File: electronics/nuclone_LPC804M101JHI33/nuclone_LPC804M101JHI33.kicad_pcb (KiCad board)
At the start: 2 copper layers, 50 x 50 mm, 42 parts, among them J1 JTAG_2X05, J2 TYPE-C-31-M-12, J3 nuclone_small_left, J4 nuclone_small_right, SW1 RESET, SW2 Bootloader, U1 MCP1702-MB, U2 TPESD0504C6

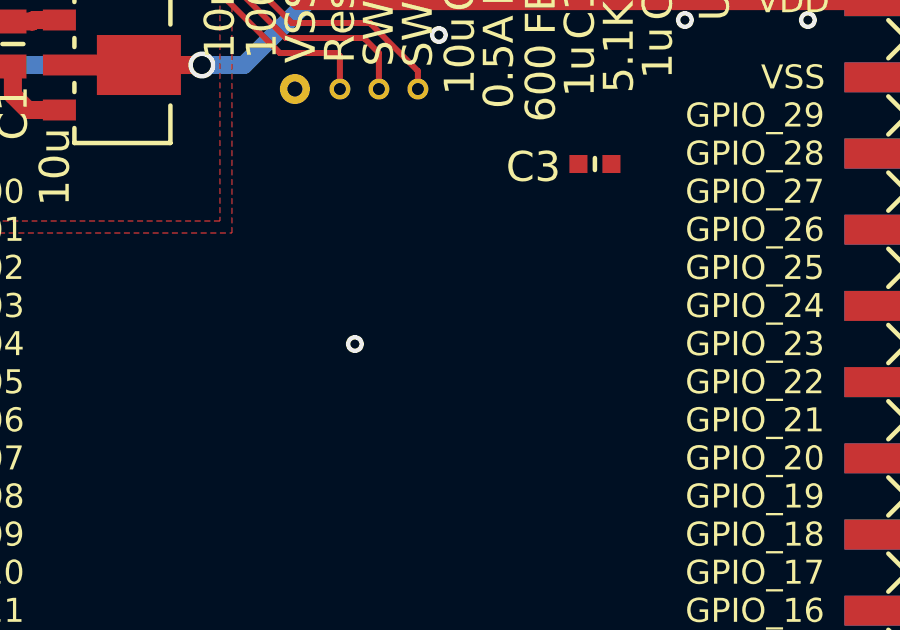
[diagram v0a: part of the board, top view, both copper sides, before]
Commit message: started schematic LPC804 nuclone
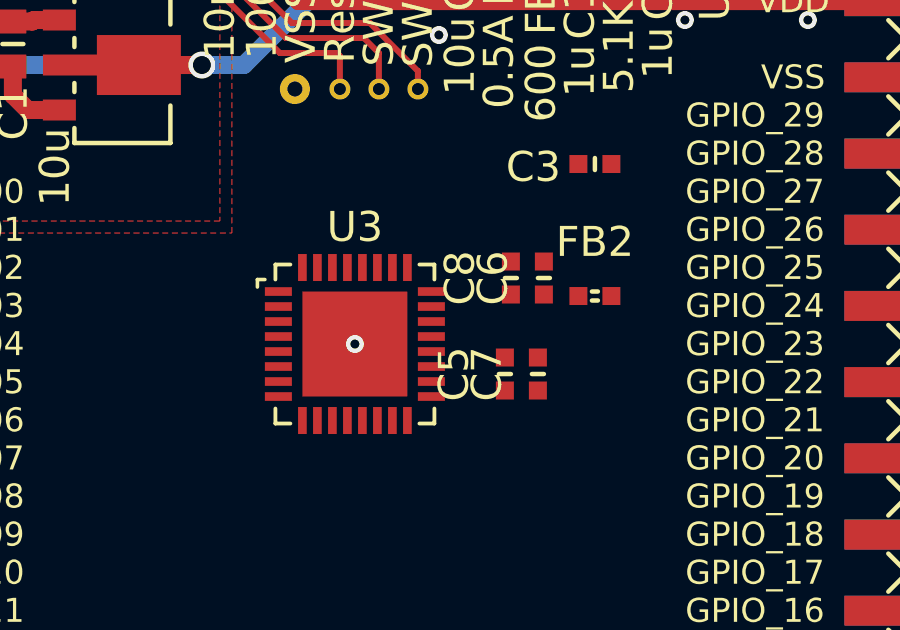
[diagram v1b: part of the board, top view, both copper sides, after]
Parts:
- added C5: 1u, SquantorRcl:C_0402, F.Cu at (90.0, 87.0)
- added C6: 1u, SquantorRcl:C_0402, F.Cu at (91.3, 83.8)
- added C7: 100n, SquantorRcl:C_0402, F.Cu at (91.1, 87.0)
- added C8: 100n, SquantorRcl:C_0402, F.Cu at (90.2, 83.8)
- added FB2: 600, SquantorRcl:L_0402, F.Cu at (93.0, 84.4)
- added U3: LPC804M101JHI33, SquantorIC:SOT617-3_alt_paste, F.Cu at (85.0, 86.0)

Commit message: WIP place and route
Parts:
- added JP1: TMS/PIO0_2, SquantorSpecial:solder_jumper_0402_2way_noconn, B.Cu at (79.8, 88.0)
- added JP2: TCK/PIO0_3, SquantorSpecial:solder_jumper_0402_2way_noconn, B.Cu at (79.8, 86.8)
- added JP3: !RESET/PIO0_5, SquantorSpecial:solder_jumper_0402_2way_noconn, B.Cu at (79.8, 85.6)
- added JP4: VDDA, SquantorSpecial:solder_jumper_0402_2way_conn, B.Cu at (85.2, 96.3)
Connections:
- net Net-(U3-Pad31) renamed /microcontroller/PIO0_18
- FB2 pad 2: /VDD -> Net-(FB2-Pad2)
- U3 pad 11: Net-(U3-Pad11) -> /GPIO_10
- U3 pad 12: Net-(U3-Pad12) -> /GPIO_11
- U3 pad 13: Net-(U3-Pad13) -> /GPIO_12
- U3 pad 14: Net-(U3-Pad14) -> /GPIO_13
- U3 pad 15: (no net) -> /GPIO_14
- U3 pad 16: Net-(U3-Pad16) -> /GPIO_15
- U3 pad 17: Net-(U3-Pad17) -> /GPIO_17
- U3 pad 18: Net-(U3-Pad18) -> /GPIO_18
- U3 pad 19: Net-(U3-Pad19) -> /GPIO_19
- U3 pad 21: Net-(U3-Pad21) -> /GPIO_20
- U3 pad 22: Net-(U3-Pad22) -> /GPIO_21
- U3 pad 24: Net-(U3-Pad24) -> /GPIO_22
- U3 pad 25: Net-(U3-Pad25) -> /GPIO_23
- U3 pad 26: Net-(U3-Pad26) -> /GPIO_24
- U3 pad 27: Net-(U3-Pad27) -> /GPIO_25
- U3 pad 28: Net-(U3-Pad28) -> /GPIO_26
- U3 pad 29: Net-(U3-Pad29) -> /GPIO_27
- U3 pad 30: Net-(U3-Pad30) -> /GPIO_28
- U3 pad 32: /microcontroller/PIO0_16 -> /GPIO_29
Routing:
- net /GPIO_02: track 0.00 -> 21.3 mm
- net /GPIO_00: track 0.00 -> 21.0 mm
- net /GPIO_04: track 0.00 -> 19.7 mm
- net /GPIO_01: track 0.00 -> 16.5 mm
- net /GPIO_03: track 0.00 -> 13.7 mm, vias 0 -> 1
- net /RESET: track 28.5 -> 40.3 mm, vias 3 -> 4
- net /VSS: vias 30 -> 34

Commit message: WIP routing
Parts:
- moved JP4 14.4 mm to (93.3, 84.5), turned to 0 degrees
- moved C5 0.40 mm to (90.4, 87.0)
- moved C7 0.40 mm to (91.5, 87.0)
- moved C6 0.28 mm to (91.5, 84.0)
- moved C8 0.28 mm to (90.4, 84.0)
- moved FB2 0.22 mm to (93.2, 84.5)
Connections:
- FB2 pad 2: Net-(FB2-Pad2) -> /microcontroller/VDDA
- U3 pad 17: /GPIO_17 -> /GPIO_16
- U3 pad 18: /GPIO_18 -> /GPIO_17
- U3 pad 19: /GPIO_19 -> /GPIO_18
- U3 pad 21: /GPIO_20 -> /GPIO_19
- U3 pad 22: /GPIO_21 -> /GPIO_20
- U3 pad 24: /GPIO_22 -> /GPIO_21
- U3 pad 25: /GPIO_23 -> /GPIO_22
- U3 pad 26: /GPIO_24 -> /GPIO_23
- U3 pad 27: /GPIO_25 -> /GPIO_24
- U3 pad 28: /GPIO_26 -> /GPIO_25
- U3 pad 29: /GPIO_27 -> /GPIO_26
- U3 pad 30: /GPIO_28 -> /GPIO_27
- U3 pad 31: /microcontroller/PIO0_18 -> /GPIO_28
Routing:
- net /GPIO_19: track 0.00 -> 21.8 mm
- net /GPIO_00: track 21.0 -> 0.00 mm
- net /GPIO_02: track 21.3 -> 0.90 mm
- net /GPIO_04: track 19.7 -> 0.00 mm
- net /GPIO_18: track 0.00 -> 18.8 mm
- net /GPIO_20: track 0.00 -> 18.4 mm
- net /GPIO_01: track 16.5 -> 0.00 mm
- net /TMS: track 20.3 -> 35.5 mm, vias 2 -> 3
- net /GPIO_03: track 13.7 -> 0.00 mm, vias 1 -> 0
- net /TCK: track 20.6 -> 34.1 mm, vias 2 -> 3
- net /VSS: track 22.0 -> 27.1 mm, vias 34 -> 36
- net /VDD: track 83.5 -> 87.6 mm
- net /microcontroller/VREFP: track 0.00 -> 4.03 mm

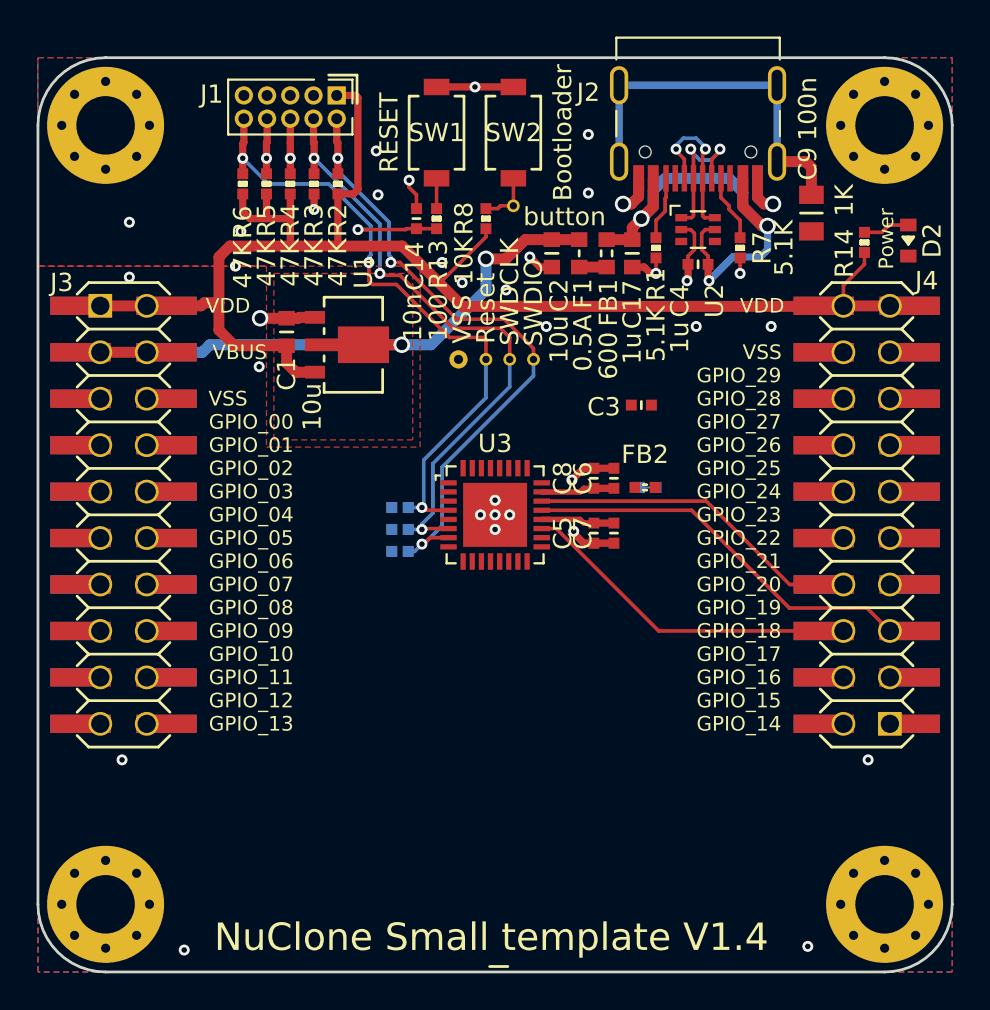
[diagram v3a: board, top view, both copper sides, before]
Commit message: updated label and further routing
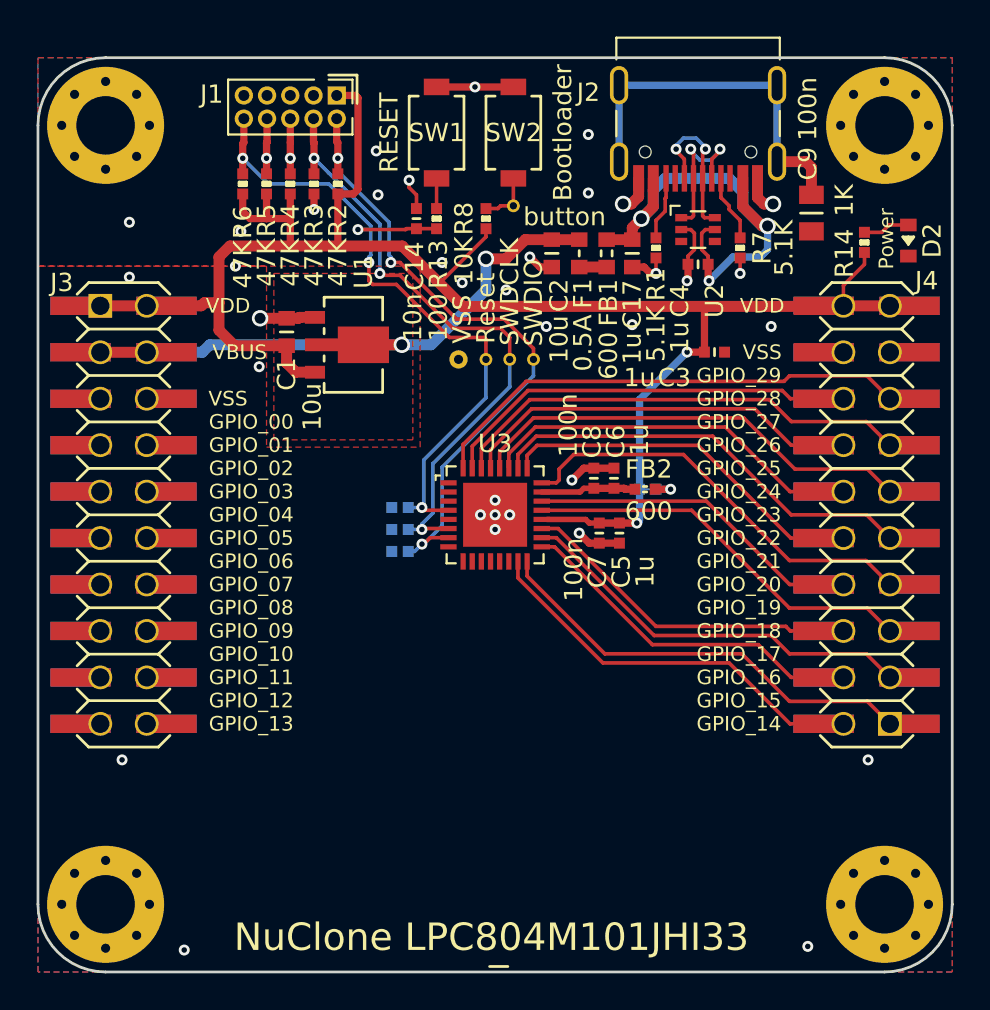
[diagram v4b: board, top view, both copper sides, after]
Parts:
- N4: value NuClone Small template V1.4 -> NuClone LPC804M101JHI33
- moved C3 4.94 mm to (97.0, 77.1), turned to 0 degrees
- moved C5 1.40 mm to (91.8, 87.0)
- moved C7 0.80 mm to (90.7, 87.0)
- moved FB2 0.10 mm to (93.2, 84.6)
- moved JP4 0.10 mm to (93.3, 84.6)
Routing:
- net /GPIO_29: track 0.00 -> 26.7 mm
- net /GPIO_27: track 0.00 -> 25.6 mm
- net /GPIO_25: track 0.00 -> 24.7 mm
- net /GPIO_15: track 0.00 -> 24.0 mm
- net /GPIO_23: track 0.00 -> 23.8 mm
- net /GPIO_21: track 0.00 -> 23.0 mm
- net /GPIO_17: track 0.00 -> 22.2 mm
- net /GPIO_28: track 0.00 -> 21.9 mm
- net /GPIO_26: track 0.00 -> 21.0 mm
- net /GPIO_14: track 0.00 -> 20.9 mm
- net /GPIO_24: track 0.00 -> 20.1 mm
- net /GPIO_22: track 0.00 -> 19.2 mm
- net /GPIO_16: track 0.00 -> 18.4 mm
- net /VDD: track 87.6 -> 102.6 mm, vias 0 -> 2
- net /microcontroller/VDDA: track 0.00 -> 1.65 mm, vias 0 -> 1
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
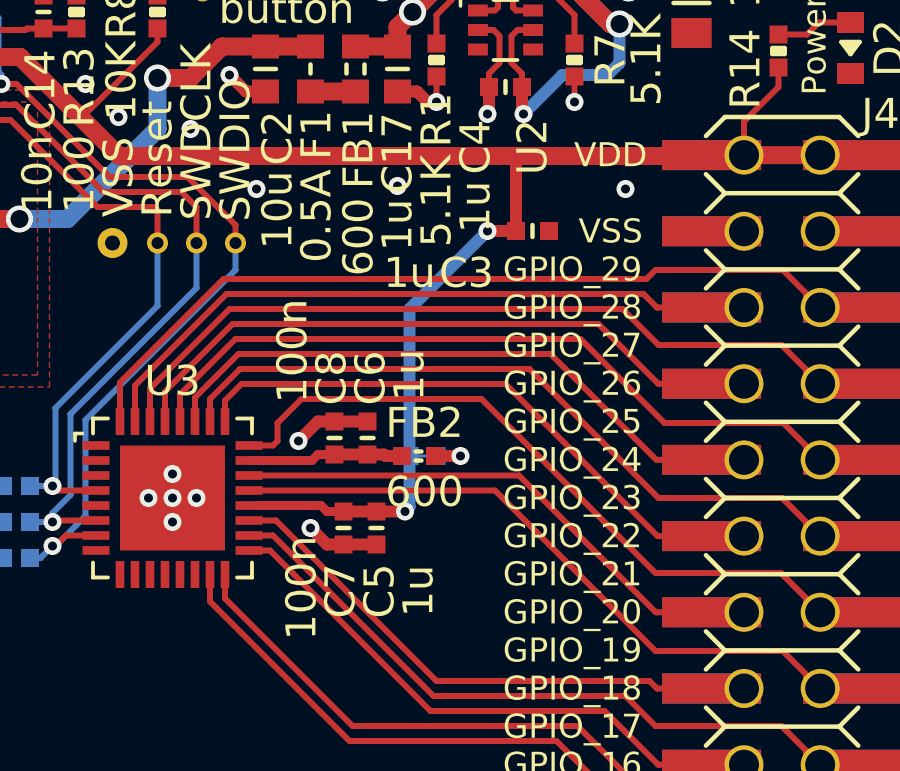
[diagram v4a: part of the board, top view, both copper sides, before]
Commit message: added ground via to fill in planes
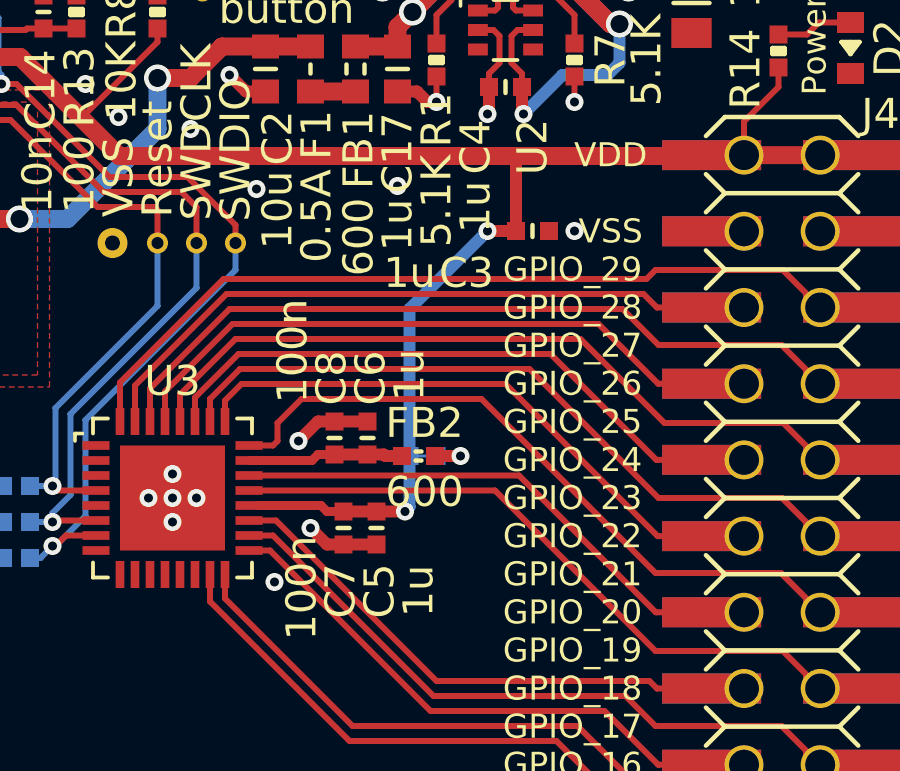
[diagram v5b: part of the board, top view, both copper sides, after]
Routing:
- net /VSS: vias 36 -> 37
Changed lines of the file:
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@@
     (thickness 1.6)
     (drawings 20)
-    (tracks 426)
+    (tracks 427)
     (zones 0)
     (modules 52)
@@
   (via (at 90.1 65.2) (size 0.6) (drill 0.3) (layers F.Cu B.Cu) (net 5))
   (via (at 90.1 68.4) (size 0.6) (drill 0.3) (layers F.Cu B.Cu) (net 5))
-  (via (at 100.1 75.7) (size 0.6) (drill 0.3) (layers F.Cu B.Cu) (net 5))
+  (via (at 98.4 77.1) (size 0.6) (drill 0.3) (layers F.Cu B.Cu) (net 5))
   (via (at 92.5 75.6) (size 0.6) (drill 0.3) (layers F.Cu B.Cu) (net 5))
   (via (at 87.8 75.7) (size 0.6) (drill 0.3) (layers F.Cu B.Cu) (net 5))
@@
   (segment (start 90.7 87.55) (end 90.15 87.55) (width 0.4) (layer F.Cu) (net 5))
   (via (at 89.6 87) (size 0.6) (drill 0.3) (layers F.Cu B.Cu) (net 5))
+  (via (at 88.4 88.8) (size 0.6) (drill 0.3) (layers F.Cu B.Cu) (net 5))
   (segment (start 101.15 79.65) (end 102.97 79.65) (width 0.2) (layer F.Cu) (net 7))
   (segment (start 100.7 79.2) (end 101.15 79.65) (width 0.2) (layer F.Cu) (net 7))

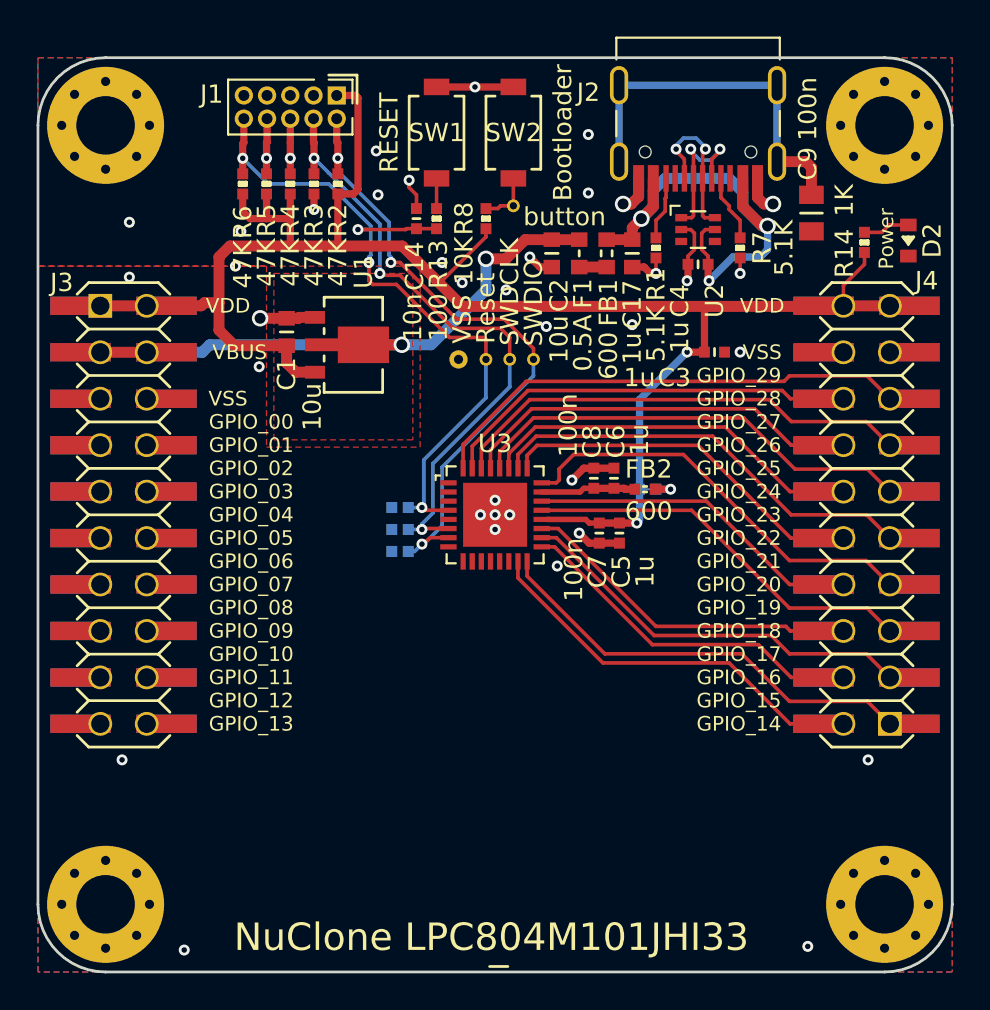
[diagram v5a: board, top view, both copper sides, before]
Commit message: routing completed, silk placement completed
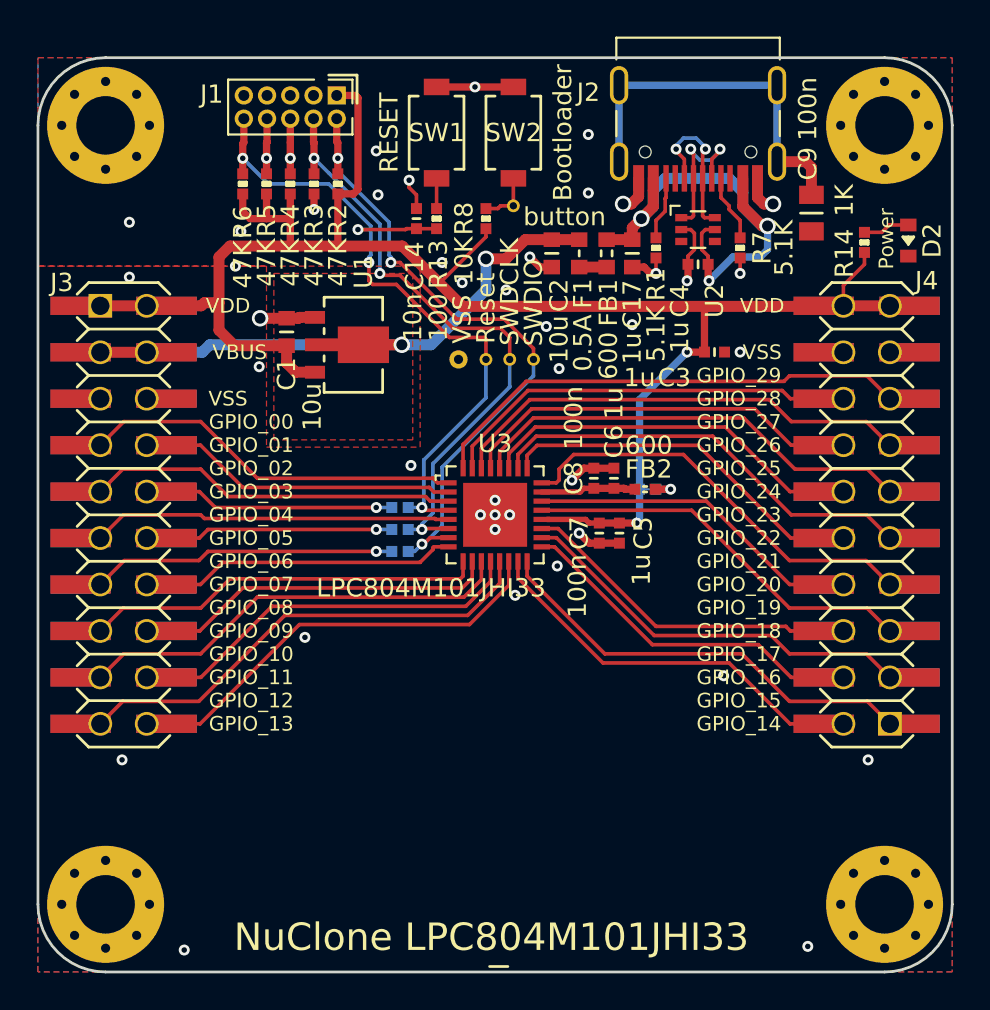
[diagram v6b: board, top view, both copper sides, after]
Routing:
- net /GPIO_12: track 0.00 -> 26.2 mm
- net /GPIO_10: track 0.00 -> 24.1 mm
- net /GPIO_13: track 0.00 -> 23.2 mm
- net /GPIO_08: track 0.00 -> 21.9 mm
- net /GPIO_11: track 0.00 -> 21.0 mm
- net /GPIO_00: track 0.00 -> 21.0 mm
- net /GPIO_02: track 0.90 -> 21.2 mm
- net /GPIO_04: track 0.00 -> 19.7 mm
- net /GPIO_09: track 0.00 -> 18.8 mm
- net /GPIO_06: track 0.00 -> 16.7 mm, vias 0 -> 1
- net /GPIO_01: track 0.00 -> 16.5 mm
- net /GPIO_07: track 0.00 -> 16.3 mm
- net /GPIO_03: track 0.00 -> 12.7 mm, vias 0 -> 1
- net /GPIO_05: track 0.00 -> 12.5 mm, vias 0 -> 1
- net /VSS: vias 37 -> 42
